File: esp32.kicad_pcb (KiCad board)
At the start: 4 copper layers, 71.5 x 36.5 mm, 50 parts, among them J1 USB_C_Receptacle_USB2.0_16P, J2 Micro_SD_Card, J3 AudioJack3, J4 BATTERY CONNECTOR, J5 Conn_01x04, SW3 SW_Push, SW4 SW_Push, SW5 SW_Push, U3 TP4056-42-ESOP8, U4 PCM5102A, U5 TPS61022, U6 ESP32-WROOM-32

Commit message: Done multiple changes here and there must for of all I routed the new parts in including the new converter for steping down power and the new smaller buttons and was able to change the board shape hahaha
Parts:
- removed C29: 2.2uF, Capacitor_SMD:C_0201_0603Metric
- removed C30, C31: 4.7uF, Capacitor_SMD:C_0201_0603Metric
- removed D2: 1N914, Diode_SMD:D_0603_1608Metric
- removed D4, D5: LED, LED_SMD:LED_0603_1608Metric
- removed J4: BATTERY CONNECTOR, Connector_JST:JST_PH_S2B-PH-K_1x02_P2.00mm_Horizontal
- removed L3: 1uH, Inductor_SMD:L_0201_0603Metric
- removed R17: 2k, Resistor_SMD:R_0201_0603Metric
- removed R18, R19, R22: 1k, Resistor_SMD:R_0201_0603Metric
- removed R20: 453k, Resistor_SMD:R_0603_1608Metric
- removed R21: 100k, Resistor_SMD:R_0603_1608Metric
- removed U3: TP4056-42-ESOP8, Package_SO:SOIC-8-1EP_3.9x4.9mm_P1.27mm_EP2.41x3.3mm_ThermalVias
- removed U5: TPS61022, Package_DFN_QFN:Texas_RWU0007A_VQFN-7_2x2mm_P0.5mm
- added C34: 10nF, Capacitor_SMD:C_0201_0603Metric, F.Cu at (154.5, 101.2)
- added D1: LED, LED_SMD:LED_0201_0603Metric, F.Cu at (141.5, 108.0)
- added L1: L, Inductor_SMD:L_0201_0603Metric, F.Cu at (138.0, 108.0)
- added R10: 100k, Resistor_SMD:R_0603_1608Metric, F.Cu at (138.0, 104.5)
- added R11: 500, Resistor_SMD:R_0603_1608Metric, F.Cu at (141.5, 105.5)
- added R9: 453, Resistor_SMD:R_0603_1608Metric, F.Cu at (138.0, 103.0)
- added U1: TLV62569ADRL, Package_TO_SOT_SMD:SOT-563, F.Cu at (138.0, 106.5)
- C19: value 100n -> 10uF
- C21: value 100nF -> 10uF
- C27: value 10uF -> 4.7uF; footprint Capacitor_SMD:C_0201_0603Metric -> Capacitor_SMD:C_0603_1608Metric
- C28: value 10uF -> 22uF; footprint Capacitor_SMD:C_0201_0603Metric -> Capacitor_SMD:C_0603_1608Metric
- D3: value LED -> 1N5817; footprint LED_SMD:LED_0603_1608Metric -> Diode_THT:D_DO-41_SOD81_P10.16mm_Horizontal
- SW3, SW4, SW5: footprint Button_Switch_SMD:SW_SPST_TL3342 -> Button_Switch_SMD:SW_Tactile_SPST_NO_Straight_CK_PTS636Sx25SMTRLFS
- moved D3 25.1 mm to (122.5, 89.8)
- moved J1 20.2 mm to (129.0, 107.5), turned to 0 degrees
- moved R7 10.2 mm to (126.5, 101.5), turned to 180 degrees
- moved J3 7.05 mm to (168.0, 103.0)
- moved R8 7.01 mm to (126.5, 100.0), turned to 180 degrees
- moved C27 4.91 mm to (136.0, 107.0), turned to 90 degrees
- moved C28 2.65 mm to (140.0, 106.7), turned to 90 degrees
- moved SW3 2.63 mm to (157.5, 104.0)
- moved SW5 1.76 mm to (152.0, 104.1), turned to 90 degrees
- moved SW4 0.14 mm to (126.5, 92.0)
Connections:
- C27 pad 1: +4.2V -> +5V
- C28 pad 1: +5V -> +3.3V
- C32 pad 2: Net-(C32-Pad2) -> GND
- D3 pad 1: Net-(D3-K) -> +5V
- D3 pad 2: +5V -> Net-(D3-A)
- J1 pad A4: Net-(D2-A) -> Net-(D3-A)
- J1 pad A9: Net-(D2-A) -> Net-(D3-A)
- J1 pad B4: Net-(D2-A) -> Net-(D3-A)
- J1 pad B9: Net-(D2-A) -> Net-(D3-A)
- SW4 pad 1: Net-(C32-Pad2) -> GND
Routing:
- net GND: track 195.1 -> 174.9 mm, vias 16 -> 20
- net Net-(D3-A): track 0.00 -> 12.8 mm
- net Net-(C32-Pad2): track 10.6 -> 0.00 mm
- net +4.2V: track 10.3 -> 0.00 mm, vias 3 -> 0
- net Net-(D5-A): track 9.74 -> 0.00 mm
- net Net-(D2-A): track 8.85 -> 0.00 mm
- net Net-(U5-SW): track 8.11 -> 0.00 mm, vias 2 -> 0
- net +5V: track 12.9 -> 5.12 mm, vias 3 -> 2
- net Net-(U4-OUTL): track 21.1 -> 13.4 mm
- net Net-(U4-OUTR): track 29.3 -> 22.1 mm
- net Net-(U4-XSMT): track 19.8 -> 12.7 mm
- net +3.3V: track 36.0 -> 42.4 mm, vias 3 -> 6
- net Net-(U3-~{STDBY}): track 6.06 -> 0.00 mm
- net Net-(U5-FB): track 5.97 -> 0.00 mm
- net /ENA: track 13.0 -> 7.91 mm
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- added copper zone on B.Cu, net GND
- added copper zone on F.Cu, net GND
- added copper zone on In1.Cu, net GND
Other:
- board size 71.5 x 36.5 mm -> 61.5 x 36.5 mm

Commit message: Added the power routing in the In2 Cu now all set to go for printing
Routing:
- added copper zone on In2.Cu, net +3.3V
- added copper zone on In2.Cu, net +5V
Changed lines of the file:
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@@
 		(tags "capacitor")
 		(property "Reference" "C26"
-			(at -2.795 -0.03 180)
+			(at 0.705 3.97 180)
 			(layer "F.SilkS")
 			(effects
@@
 		(tags "TRS audio jack stereo horizontal")
 		(property "Reference" "J3"
-			(at 0 -8.8 90)
+			(at -6.5 -6 90)
 			(layer "F.SilkS")
+			(hide yes)
 			(effects
 				(font
@@
 		)
 		(fp_text user "${REFERENCE}"
-			(at 0 -1.5 90)
+			(at -7.5 0 180)
 			(layer "F.Fab")
 			(effects
@@
 		(tags "resistor")
 		(property "Reference" "R14"
-			(at 0 2.45 180)
+			(at -0.53 1.45 180)
 			(layer "F.SilkS")
 			(effects
@@
 		(tags "capacitor")
 		(property "Reference" "C34"
-			(at 0 1 270)
+			(at -8.32 0 270)
 			(layer "F.SilkS")
 			(effects
@@
 		(tags "capacitor")
 		(property "Reference" "C24"
-			(at 2.155 -0.5 180)
+			(at 3.375 0.05 180)
 			(layer "F.SilkS")
 			(effects
@@
 		(tags "usb usb-c 2.0 pd")
 		(property "Reference" "J1"
-			(at 7 3.54 0)
+			(at -6.5 0.5 0)
 			(layer "F.SilkS")
 			(effects
@@
 		(tags "capacitor")
 		(property "Reference" "C25"
-			(at -3.935 -1.03 180)
+			(at 2.065 2.97 180)
 			(layer "F.SilkS")
 			(effects
@@
 		(tags "capacitor")
 		(property "Reference" "C33"
-			(at 2.155 0 180)
+			(at 3.375 0.55 180)
 			(layer "F.SilkS")
 			(effects
@@
 		(tags "resistor")
 		(property "Reference" "R10"
-			(at -2.9375 -0.01 0)
+			(at 5.542501 -0.01 0)
 			(layer "F.SilkS")
 			(effects
@@
 		(tags "switch tactile SPST 1P1T straight NO SMTR C&K")
 		(property "Reference" "SW3"
-			(at 4.125 2.5 0)
+			(at 6 0 0)
 			(unlocked yes)
 			(layer "F.SilkS")
@@
 		(tags "switch tactile SPST 1P1T straight NO SMTR C&K")
 		(property "Reference" "SW5"
-			(at -1.5 3.5 0)
+			(at -5.875 0 0)
 			(unlocked yes)
 			(layer "F.SilkS")
@@
 		(tags "TSSOP SO")
 		(property "Reference" "U4"
-			(at -4.6375 -1.55 90)
+			(at 5 0.3925 90)
 			(layer "F.SilkS")
 			(effects
@@
 			)
 		)
+	)
+	(zone
+		(net "+3.3V")
+		(layer "In2.Cu")
+		(hatch edge 0.5)
+		(priority 2)
+		(connect_pads
+			(clearance 0.5)
+		)
+		(min_thickness 0.25)
+		(fill yes
+			(thermal_gap 0.5)
+			(thermal_bridge_width 0.5)
+			(island_removal_mode 0)
+		)
+		(polygon
+			(pts
+				(xy 118 75.5) (xy 179.5 75.5) (xy 179.5 96) (xy 173 96) (xy 173 112) (xy 137 112) (xy 137 106.5)
+				(xy 129 106.5) (xy 128.5 89) (xy 118 89)
+			)
+		)
+	)
+	(zone
+		(net "+5V")
+		(layer "In2.Cu")
+		(hatch edge 0.5)
+		(priority 1)
+		(connect_pads
+			(clearance 0.5)
+		)
+		(min_thickness 0.25)
+		(fill yes
+			(thermal_gap 0.5)
+			(thermal_bridge_width 0.5)
+			(island_removal_mode 0)
+		)
+		(polygon
+			(pts
+				(xy 120 89) (xy 128.5 89) (xy 129 106.5) (xy 137 106.5) (xy 137 112) (xy 120 112)
+			)
+		)

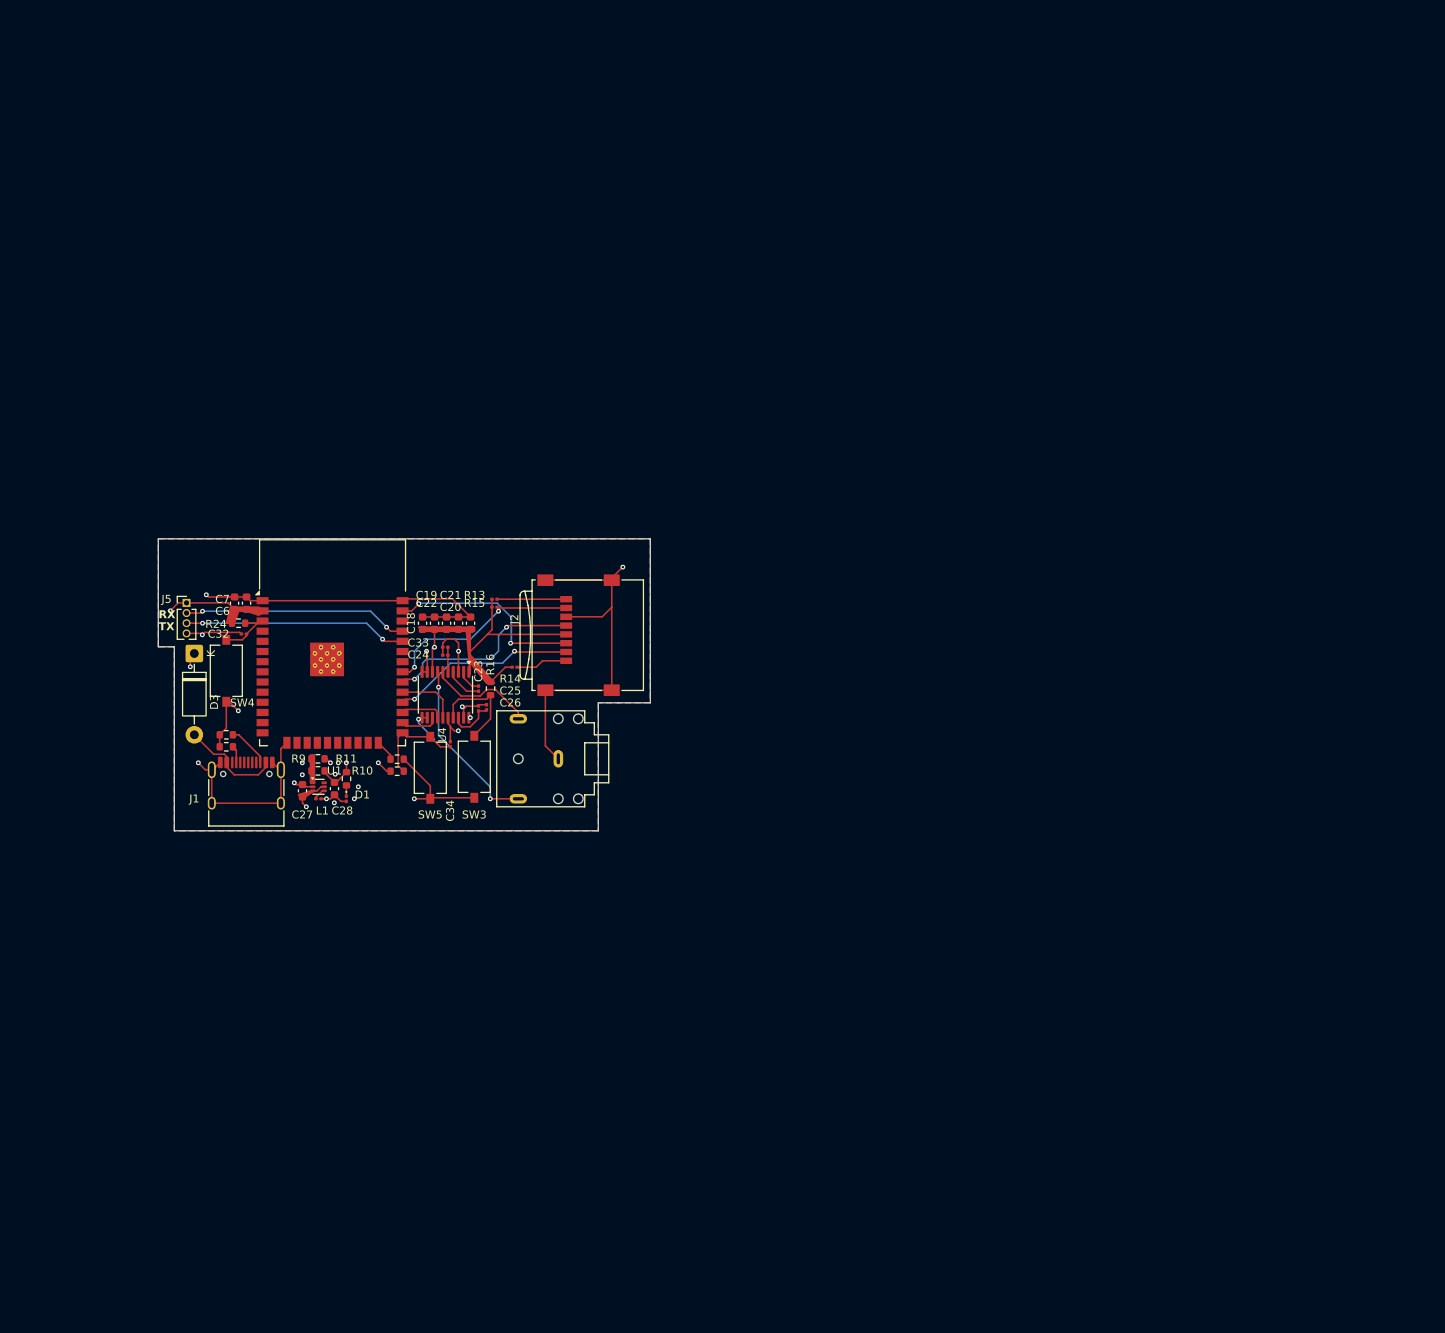
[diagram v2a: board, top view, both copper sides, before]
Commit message: Added a headphone amplifier signal and fixed the DAC converter connections based on the datasheet #almost blew it up
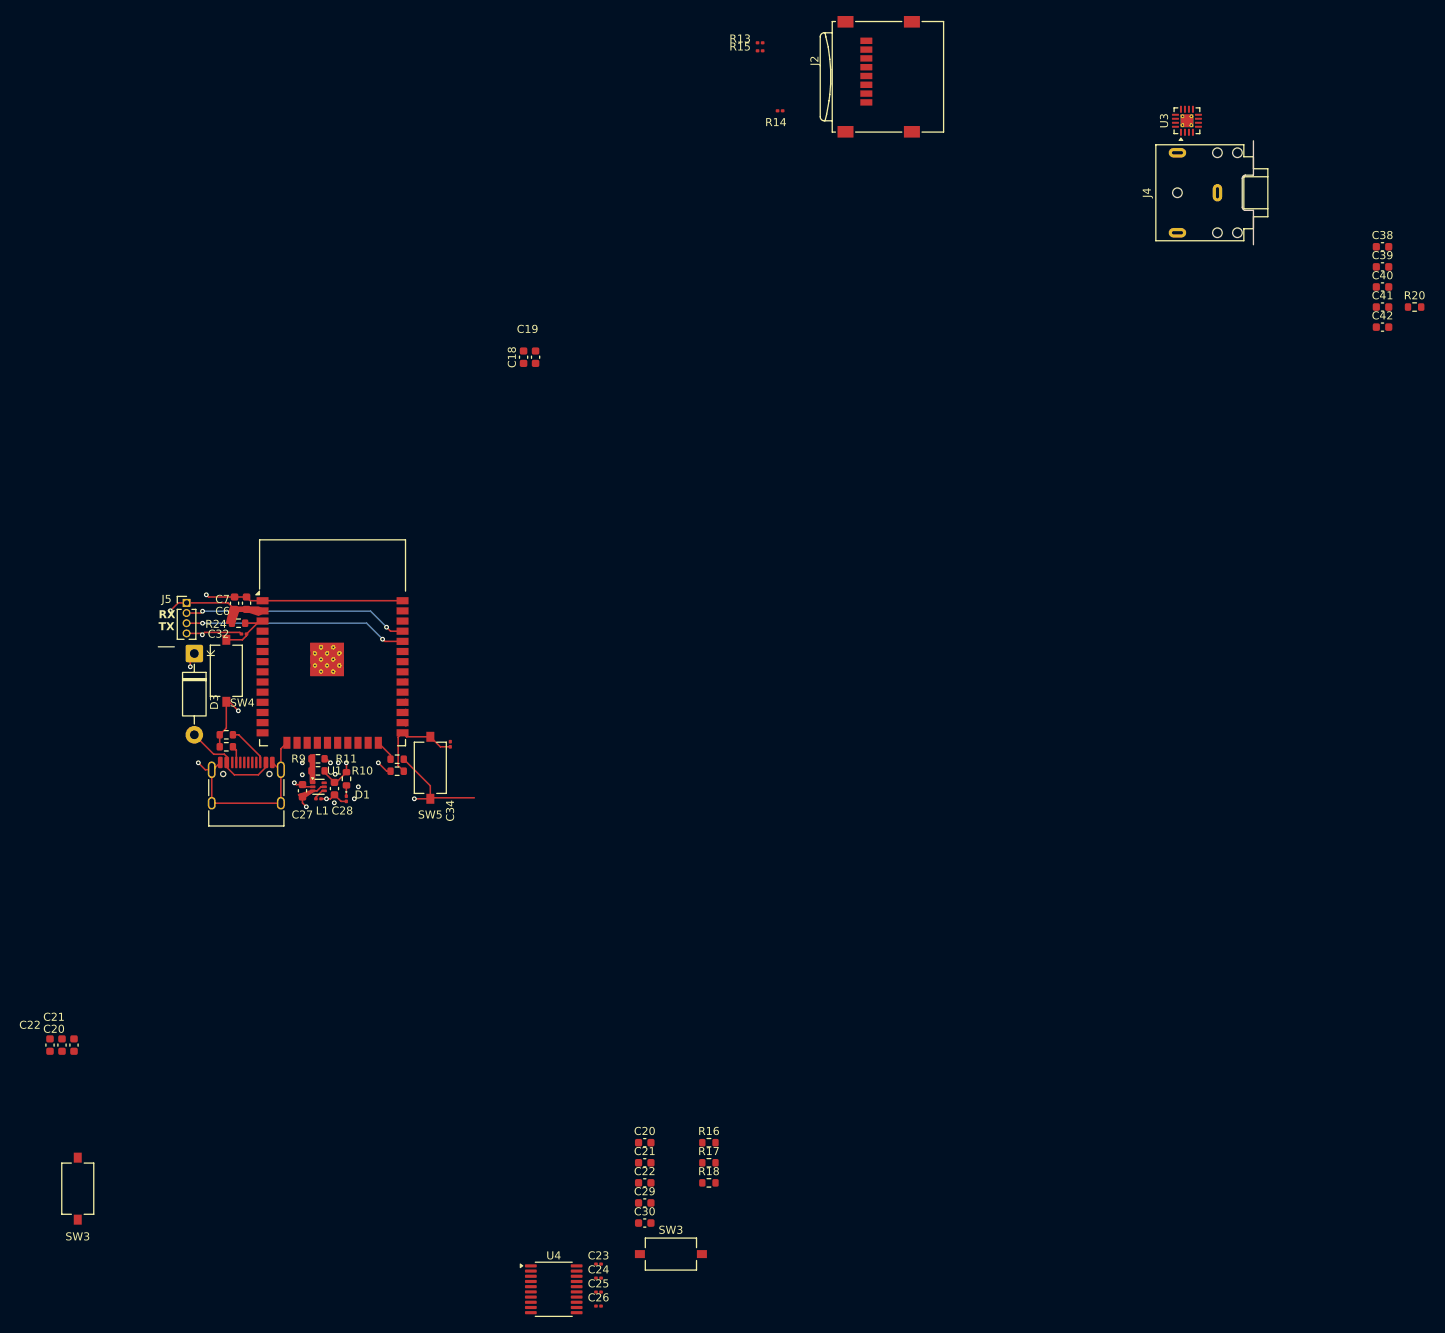
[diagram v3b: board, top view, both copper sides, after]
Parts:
- removed C33: 0.1uF, Capacitor_SMD:C_0201_0603Metric
- removed J3: AudioJack3, Connector_Audio:Jack_3.5mm_CUI_SJ1-3523N_Horizontal
- added C20: 100nF, Capacitor_SMD:C_0603_1608Metric, F.Cu at (178.8, 151.0)
- added C21: 10uF, Capacitor_SMD:C_0603_1608Metric, F.Cu at (178.8, 153.5)
- added C22: 1uF, Capacitor_SMD:C_0603_1608Metric, F.Cu at (178.8, 156.0)
- added C29: 2.2nF, Capacitor_SMD:C_0603_1608Metric, F.Cu at (178.8, 158.5)
- added C30: 2.2nF, Capacitor_SMD:C_0603_1608Metric, F.Cu at (178.8, 161.0)
- added C38: 10uF, Capacitor_SMD:C_0603_1608Metric, F.Cu at (271.0, 39.0)
- added C39: 0.1uF, Capacitor_SMD:C_0603_1608Metric, F.Cu at (271.0, 41.5)
- added C40: 1uF, Capacitor_SMD:C_0603_1608Metric, F.Cu at (271.0, 44.0)
- added C41: 2.2uF, Capacitor_SMD:C_0603_1608Metric, F.Cu at (271.0, 46.5)
- added C42: 1uF, Capacitor_SMD:C_0603_1608Metric, F.Cu at (271.0, 49.0)
- added J4: AudioJack3, Connector_Audio:Jack_3.5mm_CUI_SJ1-3523N_Horizontal, F.Cu at (250.4, 32.2)
- added R17: 0.47k, Resistor_SMD:R_0603_1608Metric, F.Cu at (186.8, 153.5)
- added R18: 0.47k, Resistor_SMD:R_0603_1608Metric, F.Cu at (186.8, 156.0)
- added R20: 10k, Resistor_SMD:R_0603_1608Metric, F.Cu at (275.0, 46.5)
- added SW3: SW_Push, Button_Switch_SMD:SW_Tactile_SPST_NO_Straight_CK_PTS636Sx25SMTRLFS, F.Cu at (182.1, 164.9)
- added U3: TPA6132A2RTE, Package_DFN_QFN:WQFN-16-1EP_3x3mm_P0.5mm_EP1.6x1.6mm_ThermalVias, F.Cu at (246.6, 23.2)
- C25: value 2.2uF -> 10uF
- L1: value L -> 1uH
- moved C24 80.2 mm to (173.0, 167.9), turned to 0 degrees
- moved J2 79.2 mm to (208.1, 17.8)
- moved R13 77.1 mm to (193.2, 13.5)
- moved R14 77.1 mm to (195.7, 22.0)
- moved R15 77.1 mm to (193.2, 14.5)
- moved C26 76.2 mm to (173.0, 171.4), turned to 0 degrees
- moved U4 75.5 mm to (167.4, 169.3), turned to 0 degrees
- moved C25 74.4 mm to (173.0, 169.7), turned to 0 degrees
- moved C23 73.5 mm to (173.0, 166.2), turned to 0 degrees
- moved C20 72.4 mm to (107.5, 138.8)
- moved C21 72.4 mm to (106.0, 138.8)
- moved C22 72.4 mm to (104.5, 138.8)
- moved SW3 72.4 mm to (107.9, 156.7)
- moved R16 63.0 mm to (186.8, 151.0), turned to 0 degrees
- moved C18 35.6 mm to (163.7, 52.8)
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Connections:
- U4 pad 13: /ESP_BCK -> /page 2/ESP_BCK
- U4 pad 14: /ESP_DIN -> /page 2/ESP_DIN
- U4 pad 15: /ESP_LRCK -> /page 2/ESP_LRCK
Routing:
- net GND: track 174.9 -> 87.2 mm, vias 20 -> 14
- net +3.3V: track 42.4 -> 15.4 mm, vias 6 -> 4
- net /ESP_MISO: track 25.6 -> 0.00 mm, vias 2 -> 0
- net /ESP_MOSI: track 25.0 -> 0.00 mm, vias 2 -> 0
- net /ESP_CK: track 25.1 -> 0.49 mm, vias 2 -> 0
- net /ESP_CS: track 23.1 -> 0.55 mm, vias 2 -> 0
- net Net-(U4-OUTR): track 22.1 -> 0.00 mm, vias 2 -> 0
- net Net-(U4-OUTL): track 13.4 -> 0.00 mm
- net Net-(U4-XSMT): track 12.7 -> 0.00 mm
- net Net-(J2-DAT1): track 8.63 -> 0.00 mm
- net /ESP_LRCK: track 7.69 -> 0.00 mm
- net Net-(J2-DAT2): track 6.46 -> 0.00 mm
- net Net-(U4-LDOO): track 5.84 -> 0.00 mm
- net /ESP_DIN: track 5.41 -> 0.54 mm
- net Net-(U4-CAPM): track 4.59 -> 0.00 mm
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- removed copper zone on In2.Cu, net +3.3V
- removed copper zone on In2.Cu, net +5V
- removed copper zone on B.Cu, net GND
- removed copper zone on F.Cu, net GND
- removed copper zone on In1.Cu, net GND
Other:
- board size 61.5 x 36.5 mm -> 1.4 x 13 mm
